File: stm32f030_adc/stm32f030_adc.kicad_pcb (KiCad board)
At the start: 2 copper layers, 39 parts, among them Q1 BC337, U1 STM32F103C6Tx, U2 AMS1117-3.3, X1 USB_B_Micro, Y2 8 MHz

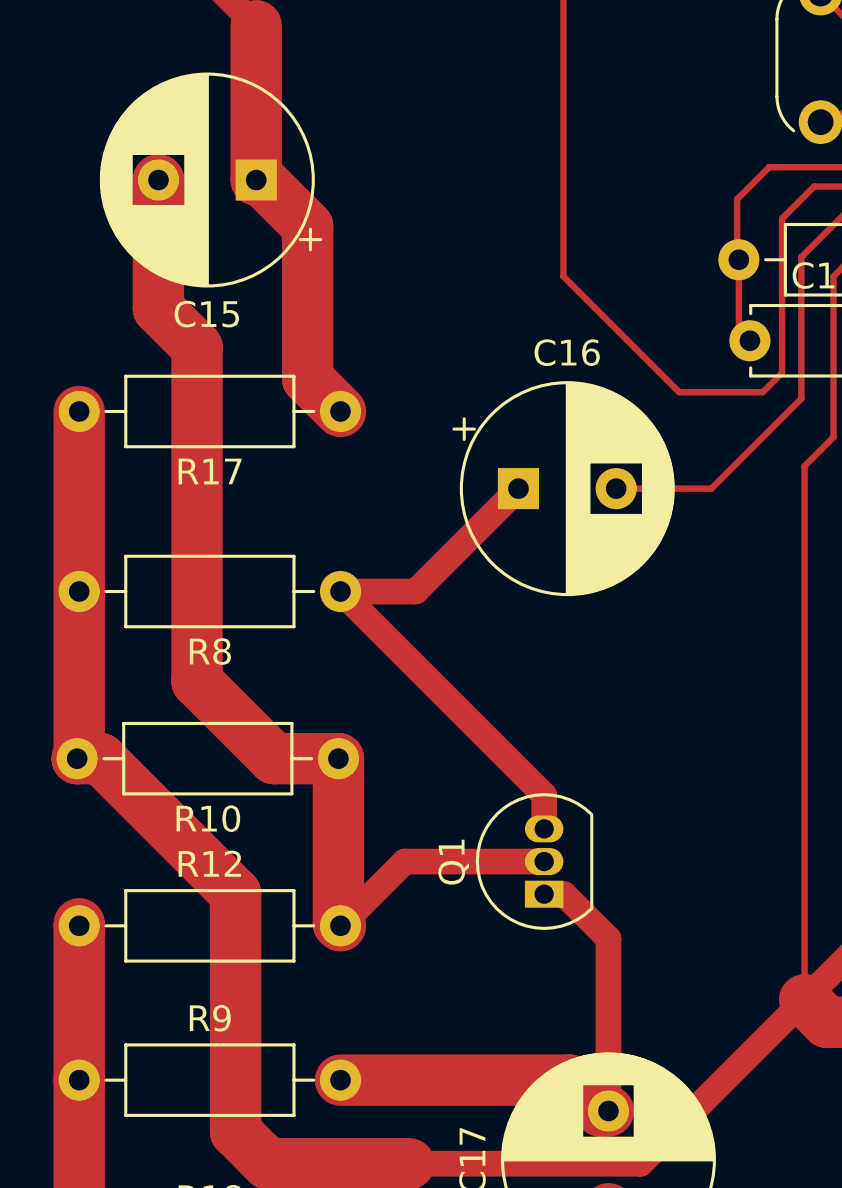
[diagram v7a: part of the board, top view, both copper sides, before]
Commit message: [schematics] Impl |  Extensibility: more 0-jumpers
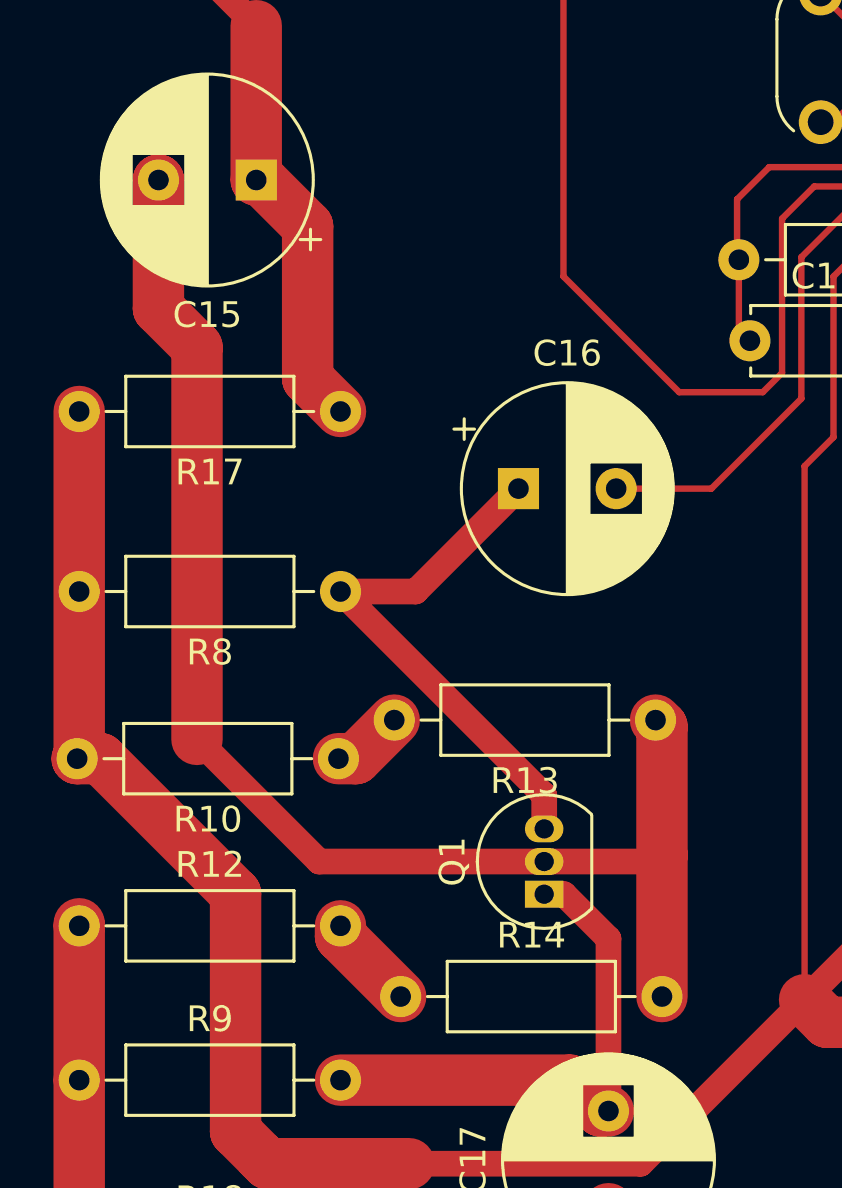
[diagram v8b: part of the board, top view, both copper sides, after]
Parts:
- added R13: 0, Resistor_THT:R_Axial_DIN0207_L6.3mm_D2.5mm_P10.16mm_Horizontal, F.Cu at (136.6, 118.0)
- added R14: 0, Resistor_THT:R_Axial_DIN0207_L6.3mm_D2.5mm_P10.16mm_Horizontal, F.Cu at (126.7, 128.8)
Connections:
- R10 pad 1: Net-(Q1-B) -> Net-(R10-Pad1)
- R12 pad 2: Net-(Q1-B) -> Net-(R12-Pad2)
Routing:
- net Net-(Q1-B): track 42.4 -> 53.4 mm
- net Net-(R12-Pad2): track 0.00 -> 3.72 mm
- net Net-(R10-Pad1): track 0.00 -> 2.79 mm
